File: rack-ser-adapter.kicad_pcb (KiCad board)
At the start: 2 copper layers, 34 x 71 mm, 8 parts, among them J1 RS-232, J2 RJ45_Shielded, J3 RS-232, J4 RJ45_Shielded

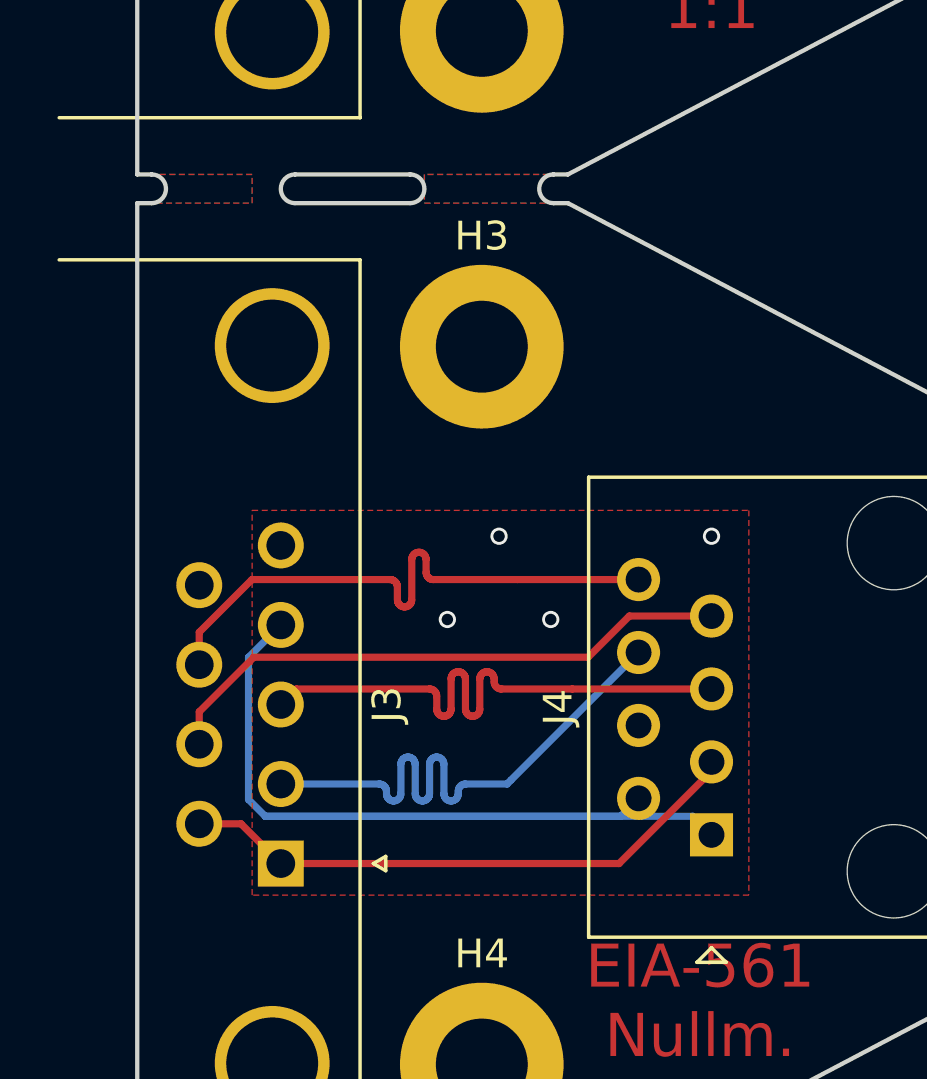
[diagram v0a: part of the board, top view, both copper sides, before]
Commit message: Update to KiCAD 10
Signed-off-by: Benedikt Spranger <b.spranger@linutronix.de>
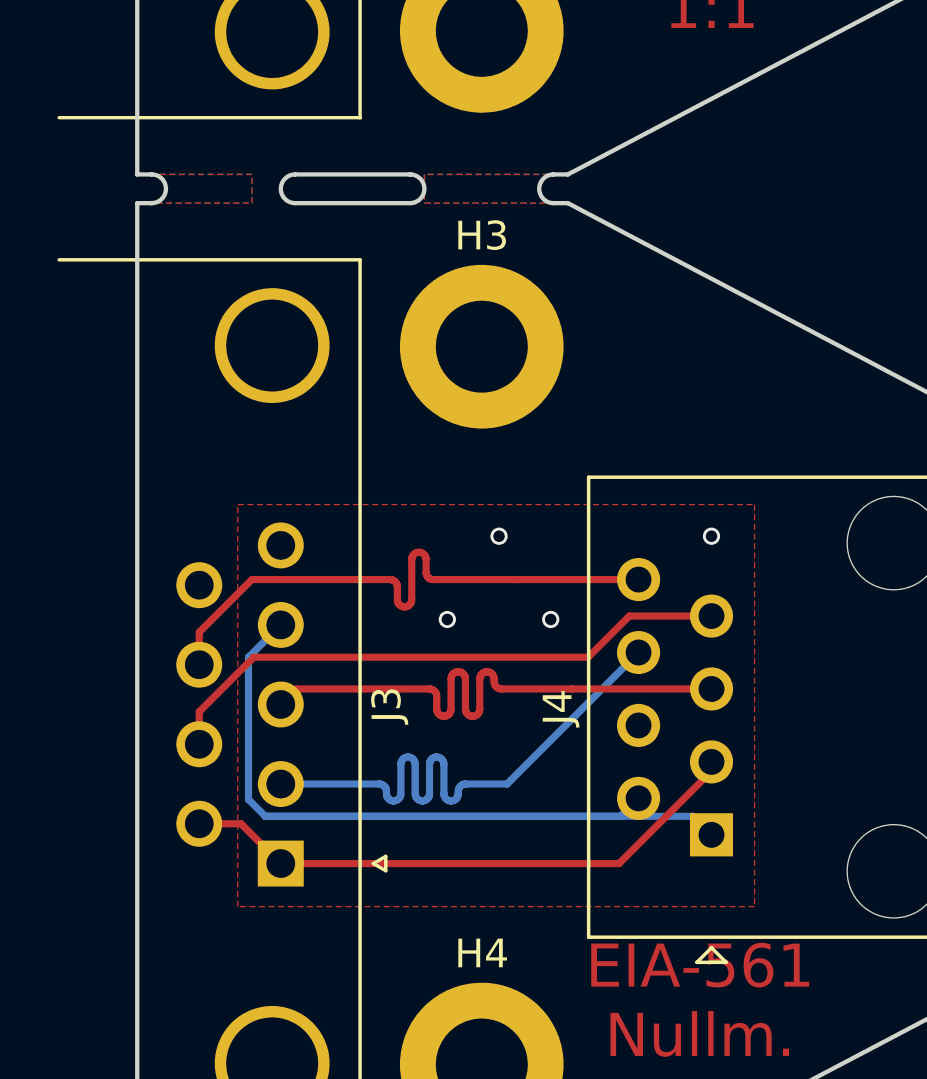
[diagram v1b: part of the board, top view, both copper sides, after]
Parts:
- J1: footprint Connector_Dsub:DSUB-9_Male_Horizontal_P2.77x2.84mm_EdgePinOffset4.94mm_Housed_MountingHolesOffset7.48mm -> Connector_Dsub_v5:DSUB-9_Male_Horizontal_P2.77x2.84mm_EdgePinOffset4.94mm_Housed_MountingHolesOffset7.48mm
- J3: footprint Connector_Dsub:DSUB-9_Female_Horizontal_P2.77x2.84mm_EdgePinOffset4.94mm_Housed_MountingHolesOffset7.48mm -> Connector_Dsub_v5:DSUB-9_Female_Horizontal_P2.77x2.84mm_EdgePinOffset4.94mm_Housed_MountingHolesOffset7.48mm
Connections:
- J1 pad 0: /SH -> (no net)
- J1 pad 9: (no net) -> unconnected-(J1-Pad9)
- J3 pad 0: /SH -> (no net)
- J3 pad 9: (no net) -> unconnected-(J3-Pad9)
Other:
- net class Default removed
